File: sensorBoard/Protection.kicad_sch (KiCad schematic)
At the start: 8 parts

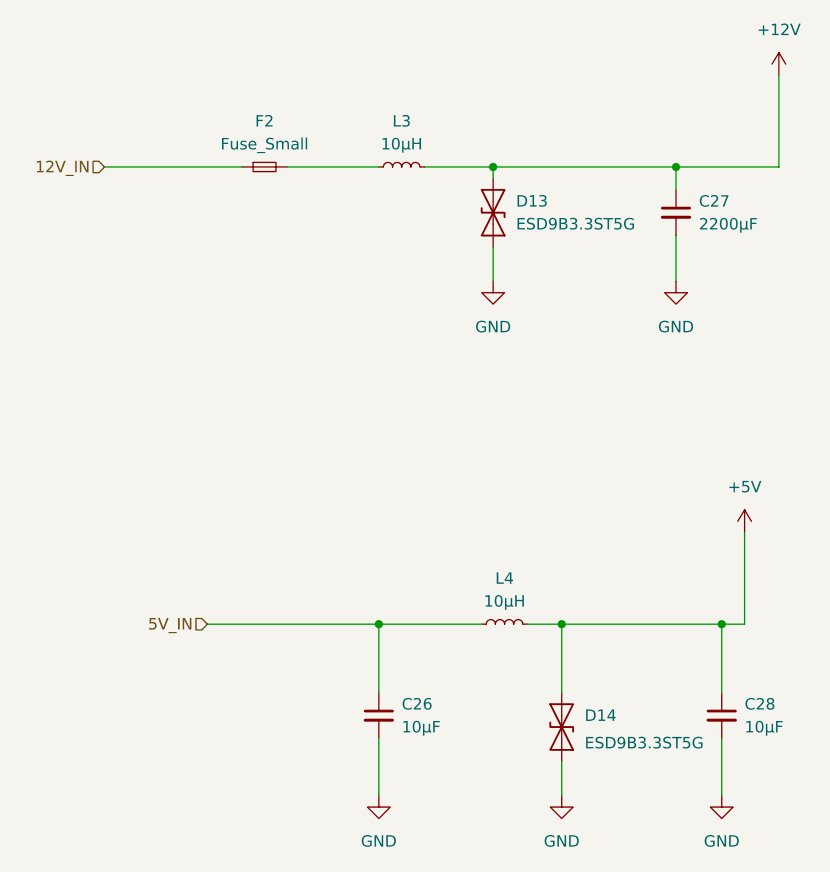
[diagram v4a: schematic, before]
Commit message: Das erstes PCB ist fast fertig. Die Vias waren auf die Platine platziert und Poligon war gefüllt.
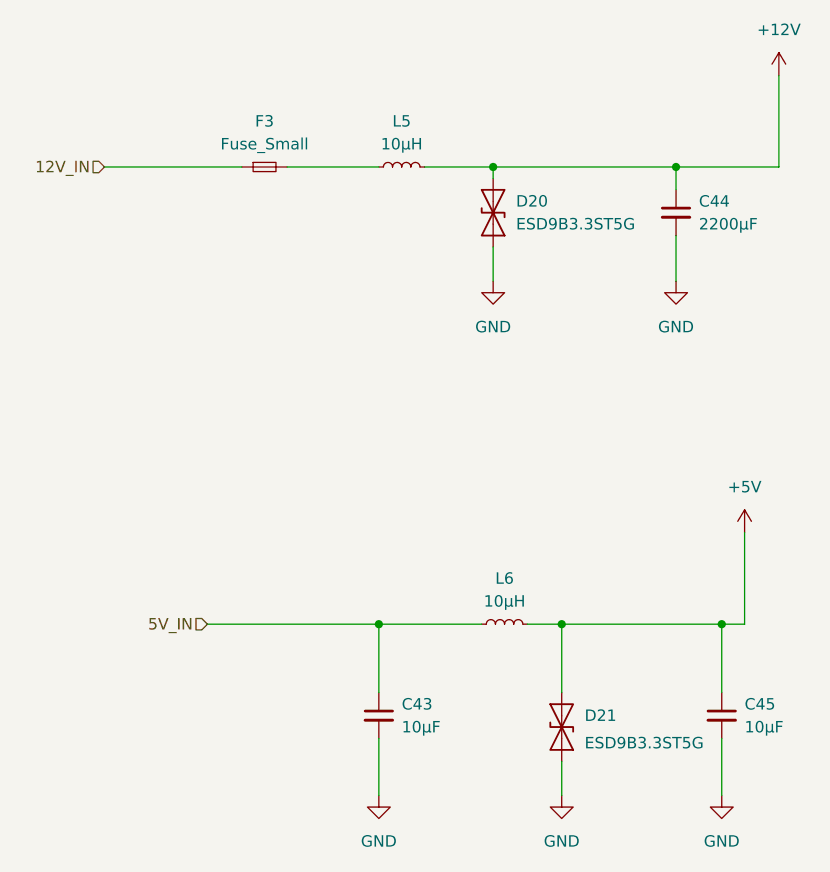
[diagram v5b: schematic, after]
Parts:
- renumbered C26 to C43, C27 to C44, C28 to C45, D13 to D20, D14 to D21, F2 to F3, L3 to L5, L4 to L6
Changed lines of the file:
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@@
 		(dnp no)
 		(fields_autoplaced yes)
-		(property "Reference" "L4"
+		(property "Reference" "L6"
 			(at 107.95 96.52 90)
 			(effects
@@
 		(dnp no)
 		(fields_autoplaced yes)
-		(property "Reference" "#PWR0128"
+		(property "Reference" "#PWR0210"
 			(at 132.08 127 0)
 			(effects
@@
 		(dnp no)
 		(fields_autoplaced yes)
-		(property "Reference" "C28"
+		(property "Reference" "C45"
 			(at 134.62 110.4962 0)
 			(effects
@@
 		(dnp no)
 		(fields_autoplaced yes)
-		(property "Reference" "#PWR0130"
+		(property "Reference" "#PWR0212"
 			(at 138.43 44.45 0)
 			(effects
@@
 		(on_board yes)
 		(dnp no)
-		(property "Reference" "D14"
+		(property "Reference" "D21"
 			(at 116.84 111.7599 90)
 			(effects
@@
 		(dnp no)
 		(fields_autoplaced yes)
-		(property "Reference" "#PWR0127"
+		(property "Reference" "#PWR0209"
 			(at 127 69.85 0)
 			(effects
@@
 		(dnp no)
 		(fields_autoplaced yes)
-		(property "Reference" "L3"
+		(property "Reference" "L5"
 			(at 96.52 45.72 90)
 			(effects
@@
 		(dnp no)
 		(fields_autoplaced yes)
-		(property "Reference" "#PWR0124"
+		(property "Reference" "#PWR0206"
 			(at 93.98 127 0)
 			(effects
@@
 		(dnp no)
 		(fields_autoplaced yes)
-		(property "Reference" "D13"
+		(property "Reference" "D20"
 			(at 109.22 54.6099 90)
 			(effects
@@
 		(dnp no)
 		(fields_autoplaced yes)
-		(property "Reference" "#PWR0126"
+		(property "Reference" "#PWR0208"
 			(at 114.3 127 0)
 			(effects
@@
 		(dnp no)
 		(fields_autoplaced yes)
-		(property "Reference" "#PWR0125"
+		(property "Reference" "#PWR0207"
 			(at 106.68 69.85 0)
 			(effects
@@
 		(dnp no)
 		(fields_autoplaced yes)
-		(property "Reference" "C26"
+		(property "Reference" "C43"
 			(at 96.52 110.4962 0)
 			(effects
@@
 		(dnp no)
 		(fields_autoplaced yes)
-		(property "Reference" "#PWR0129"
+		(property "Reference" "#PWR0211"
 			(at 134.62 95.25 0)
 			(effects
@@
 		(dnp no)
 		(fields_autoplaced yes)
-		(property "Reference" "C27"
+		(property "Reference" "C44"
 			(at 129.54 54.6162 0)
 			(effects
@@
 		(dnp no)
 		(fields_autoplaced yes)
-		(property "Reference" "F2"
+		(property "Reference" "F3"
 			(at 81.28 45.72 0)
 			(effects

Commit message: finisched PCB
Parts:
- L5: footprint Inductor_SMD:L_Coilcraft_XAL1580-612 -> Inductor_SMD:L_Wuerth_HCI-1890
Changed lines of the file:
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@@
 			)
 		)
-		(property "Footprint" "Inductor_SMD:L_Coilcraft_XAL1580-612"
+		(property "Footprint" "Inductor_SMD:L_Wuerth_HCI-1890"
 			(at 96.52 50.8 0)
 			(effects
@@
 			)
 		)
-		(property "Datasheet" "https://www.mouser.de/ProductDetail/Wurth-Elektronik/78439370100?qs=Znm5pLBrcALJdf%2F0qW3A9g%3D%3D"
+		(property "Datasheet" "https://www.mouser.de/ProductDetail/Wurth-Elektronik/74435561100?qs=MVRUG6Lt7nEAbWWCpRhe%2FA%3D%3D"
 			(at 96.52 50.8 0)
 			(effects
